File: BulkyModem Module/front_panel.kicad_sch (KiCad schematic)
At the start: 24 parts, among them J3 Module_Panel, U5 74HCT04

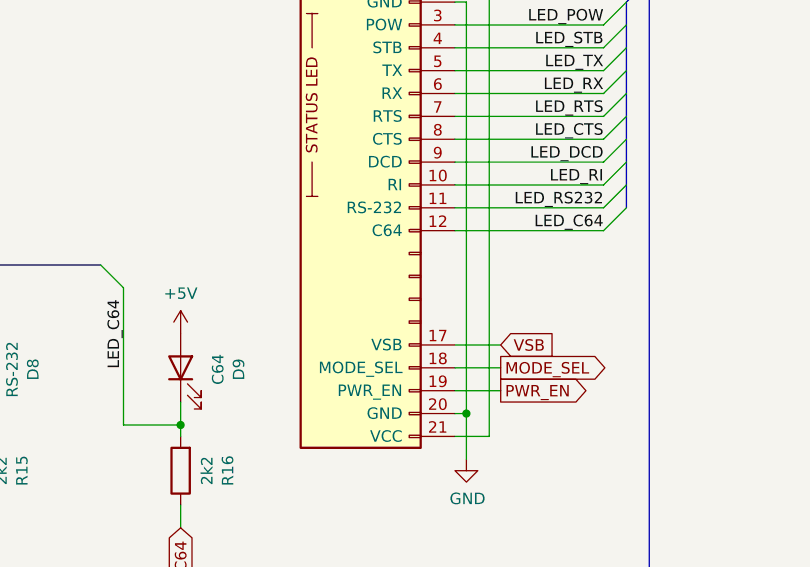
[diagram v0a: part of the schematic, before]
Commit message: Add mounting points for audio module
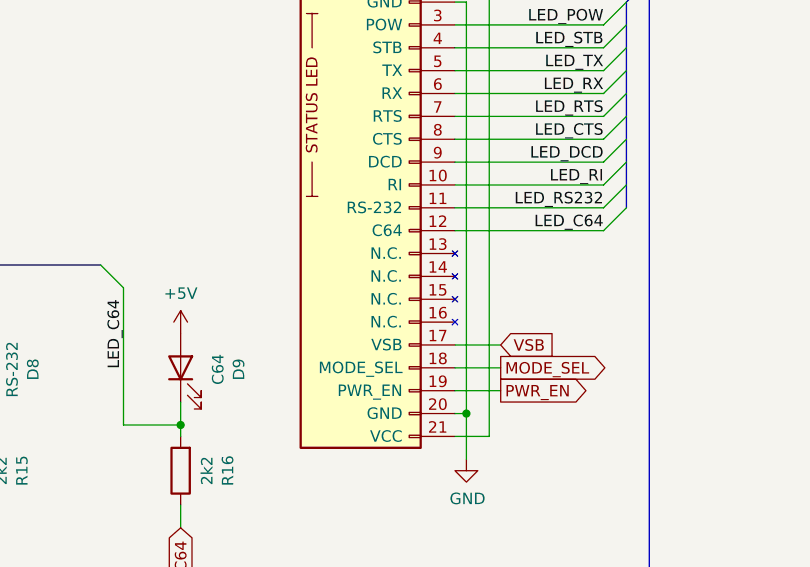
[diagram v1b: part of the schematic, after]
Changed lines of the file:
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@@
 		(pin "15"
+		)
+		(instances
+			(project "BulkyModem Module"
+				(path "/cd9da885-84b5-47eb-b16d-d4099ea4358c/00000000-0000-0000-0000-00006390ae73"
+					(reference "J3")
+					(unit 1)
+				)
+			)
 		)
 	)

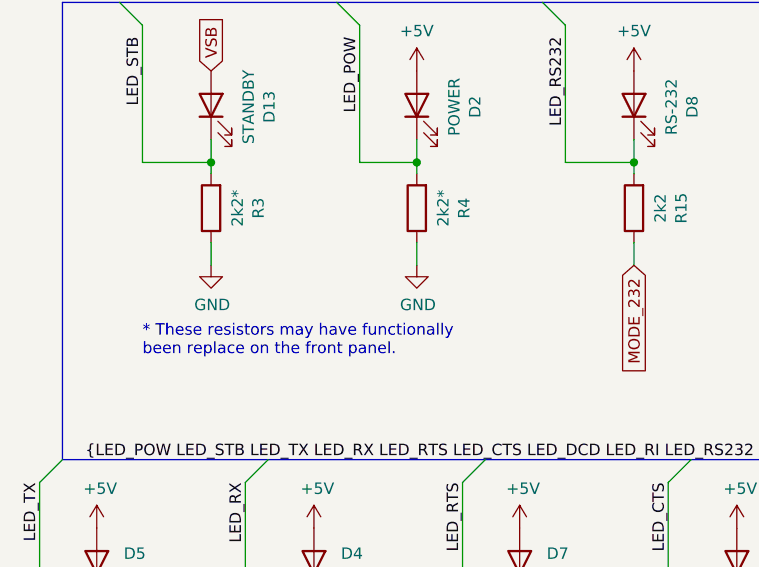
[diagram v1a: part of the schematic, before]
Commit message: Add labels to LEDs
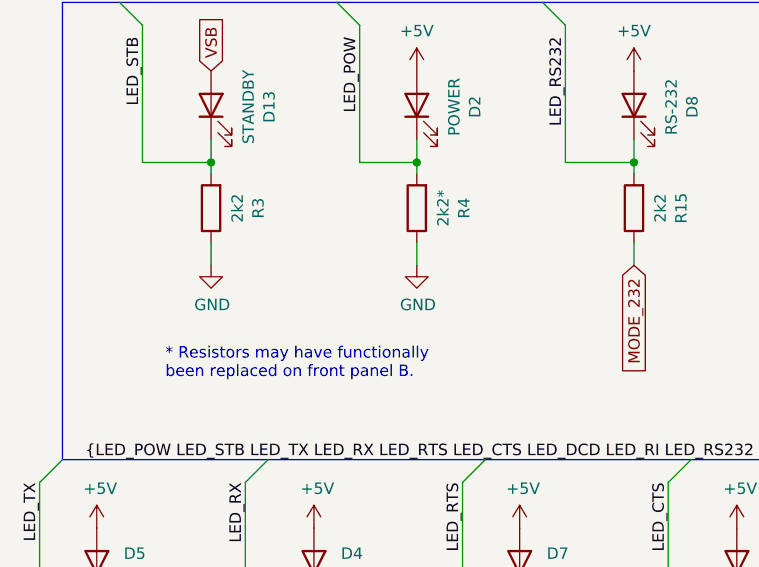
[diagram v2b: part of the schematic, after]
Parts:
- R3: value 2k2* -> 2k2
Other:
- note added: "* Resistors may have functionally been replaced on front panel B."
- note removed: "* These resistors may have functionally been replace on the front panel."
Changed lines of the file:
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@@
 		)
 	)
-	(text "* These resistors may have functionally\nbeen replace on the front panel."
+	(text "* Resistors may have functionally\nbeen replaced on front panel B."
 		(exclude_from_sim no)
-		(at 45.72 100.33 0)
+		(at 48.26 102.87 0)
 		(effects
 			(font
@@
 			)
 		)
-		(property "Value" "2k2*"
+		(property "Value" "2k2"
 			(at 56.2864 83.82 90)
 			(effects
